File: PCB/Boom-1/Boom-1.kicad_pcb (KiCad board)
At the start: 2 copper layers, 698 parts, among them J1 NoiseIOConn, J10 Osc1HFTrackConn, J11 Osc1FiltCVConn, J12 OscFiltEnv1Conn, J13 OscFiltEnv2Conn, J14 SubFiltEnv1Conn, J15 SubFiltEnv2Conn, J16 Osc1FXConn, J17 SubFXConn, J18 Osc1FiltCVConn, J19 Osc1FiltCVConn, J2 Osc2CVConn, J20 Osc2FXConn, J21 OscAmpEnvConn, J22 SubAmpEnvConn, J23 OscAmpEnvBypass, J24 SubAmpAudioBypass, J25 SubAmpEnvBypass, J26 PreFV1FXConn, J27 PowerConn, J28 FV1Conn, J29 IOConn, J3 Osc1CVConn, J4 Osc2SyncConn, J5 Osc1SyncConn, J6 Osc2ScaleConn, J7 Osc2HFTrackConn, J8 SubIOConn, J9 Osc1ScaleConn, Q1 2N3904, SW1 SW_DIP_x04, U1 CEM3340, U10 AS3320, U11 AS3310, U12 AS3310, U13 AS3310, U14 AS3310, U15 V2164D, U16 AS3310, U17 AS3310, U18 V2164D, U19 TL074, U2 CEM3340, U20 TL074, U21 TL074, U22 TL074, U23 TL074, U24 TL074, U25 TL074, U26 TL074, U27 TL072, U28 TL074, U29 TL072, U3 4013, U30 TL074, U31 TL072, U32 TL074, U33 TL074, U34 TL074, U35 TL072, U36 TL074, U37 TL074, U38 TL072, U39 TL074, U4 NOISE, U40 TL072, U41 TL074, U42 TL074, U43 TL074, U44 TL074, U45 L7905, U46 L7805, U5 V2164D, U6 V2164D, U7 V2164D, U8 AS3320, U9 AS3320

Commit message: gathered up some stray parts
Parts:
- moved TP4 1583.4 mm to (-734.3, 189.5)
- moved R79 1444.9 mm to (-708.9, 138.4)
- moved R80 1426.5 mm to (-724.4, 378.7)
- moved R57 1421.4 mm to (-736.3, 372.4)
- moved R56 1403.7 mm to (-729.2, 369.1)
- moved R58 1394.2 mm to (-736.6, 378.7)
- moved R370 1292.9 mm to (-721.6, 403.1), turned to 180 degrees
- moved R292 813.4 mm to (2.29, 146.6)
- moved C106 42.6 mm to (751.1, 644.7)
- moved C138 42.6 mm to (754.9, 661.1)
- moved C148 42.6 mm to (769.2, 635.3)
- moved C149 42.6 mm to (767.9, 644.5)
- moved C163 42.6 mm to (735.1, 647.7)
- moved C171 42.6 mm to (736.0, 643.5)
- moved C40 42.6 mm to (764.0, 640.0)
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
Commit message: gathered up some rogue parts, started on the FX section components - pausing to update from schema
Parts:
- moved C41 1813.5 mm to (-730.5, -367.8)
- moved C40 1804.8 mm to (-721.1, -385.6)
- moved R100 1751.0 mm to (-739.1, -370.8)
- moved R131 1737.4 mm to (-691.9, -406.0)
- moved R99 1726.2 mm to (-728.5, -379.7)
- moved R186 1515.2 mm to (-483.9, -302.3)
- moved C54 1412.1 mm to (-400.6, -123.4)
- moved R142 1341.1 mm to (-403.6, -117.6)
- moved C111 1317.7 mm to (-503.2, 255.5), turned to 180 degrees
- moved R181 1309.8 mm to (-366.8, -99.8), turned to 180 degrees
- moved C112 1264.4 mm to (-483.6, 345.9), turned to 270 degrees
- moved C106 1243.8 mm to (-457.5, 350.8)
- moved C107 1240.9 mm to (-440.2, 350.8)
- moved C110 1233.3 mm to (-473.5, 249.4), turned to 270 degrees
- moved C101 1230.8 mm to (-439.9, 296.4)
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
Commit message: all parts are gathered from the swamp
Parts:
- moved C18 1357.0 mm to (-716.5, -341.5)
- moved C19 1289.3 mm to (-696.5, -345.1)
- moved C12 1270.9 mm to (-715.6, -132.0)
- moved C24 1248.0 mm to (-698.1, -102.5)
- moved C23 1225.3 mm to (-716.0, -100.7)
- moved C13 1217.0 mm to (-698.5, -132.1)
- moved C147 315.7 mm to (278.5, 27.9), turned to 90 degrees
- moved C149 311.5 mm to (295.0, 9.02), turned to 270 degrees
- moved R338 275.9 mm to (408.9, 18.3)
- moved R340 269.2 mm to (386.5, 1.40)
- moved R327 267.8 mm to (323.5, 0.00), turned to 180 degrees
- moved R365 263.7 mm to (511.2, 11.6)
- moved R337 259.9 mm to (410.7, 23.5)
- moved C172 258.9 mm to (496.1, 3.17), turned to 180 degrees
- moved R342 254.7 mm to (395.4, 6.99)
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
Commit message: osc1 layout
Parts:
- moved R109 79.6 mm to (-741.3, -358.9)
- moved D10 77.5 mm to (334.3, -67.9), turned to 90 degrees
- moved TP20 74.1 mm to (-750.1, -329.2)
- moved TP21 66.6 mm to (-746.0, -329.2)
- moved R371 61.1 mm to (-733.7, -347.6), turned to 180 degrees
- moved R114 59.7 mm to (-754.5, -343.0), turned to 180 degrees
- moved C43 51.4 mm to (-738.1, -369.2), turned to 270 degrees
- moved R85 51.3 mm to (-772.9, -404.4)
- moved R108 51.3 mm to (-741.3, -334.8)
- moved TP18 48.7 mm to (-746.4, -365.8)
- moved R132 48.5 mm to (-742.2, -409.4)
- moved R130 48.3 mm to (-744.5, -390.9)
- moved C51 48.2 mm to (-739.6, -406.1)
- moved U5 47.8 mm to (-751.7, -355.7)
- moved C41 47.7 mm to (-758.1, -328.8), turned to 90 degrees
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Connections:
- C51 pad 2: Net-(C51-Pad1) -> Net-(C51-Pad2)
- R108 pad 2: Net-(C51-Pad1) -> Net-(C51-Pad2)
- R109 pad 2: Net-(C51-Pad1) -> Net-(C51-Pad2)
- R132 pad 1: Net-(C51-Pad1) -> Net-(C51-Pad2)
- TP26 pad 1: Net-(C51-Pad1) -> Net-(C51-Pad2)
- U19 pad 14: Net-(C51-Pad1) -> Net-(C51-Pad2)

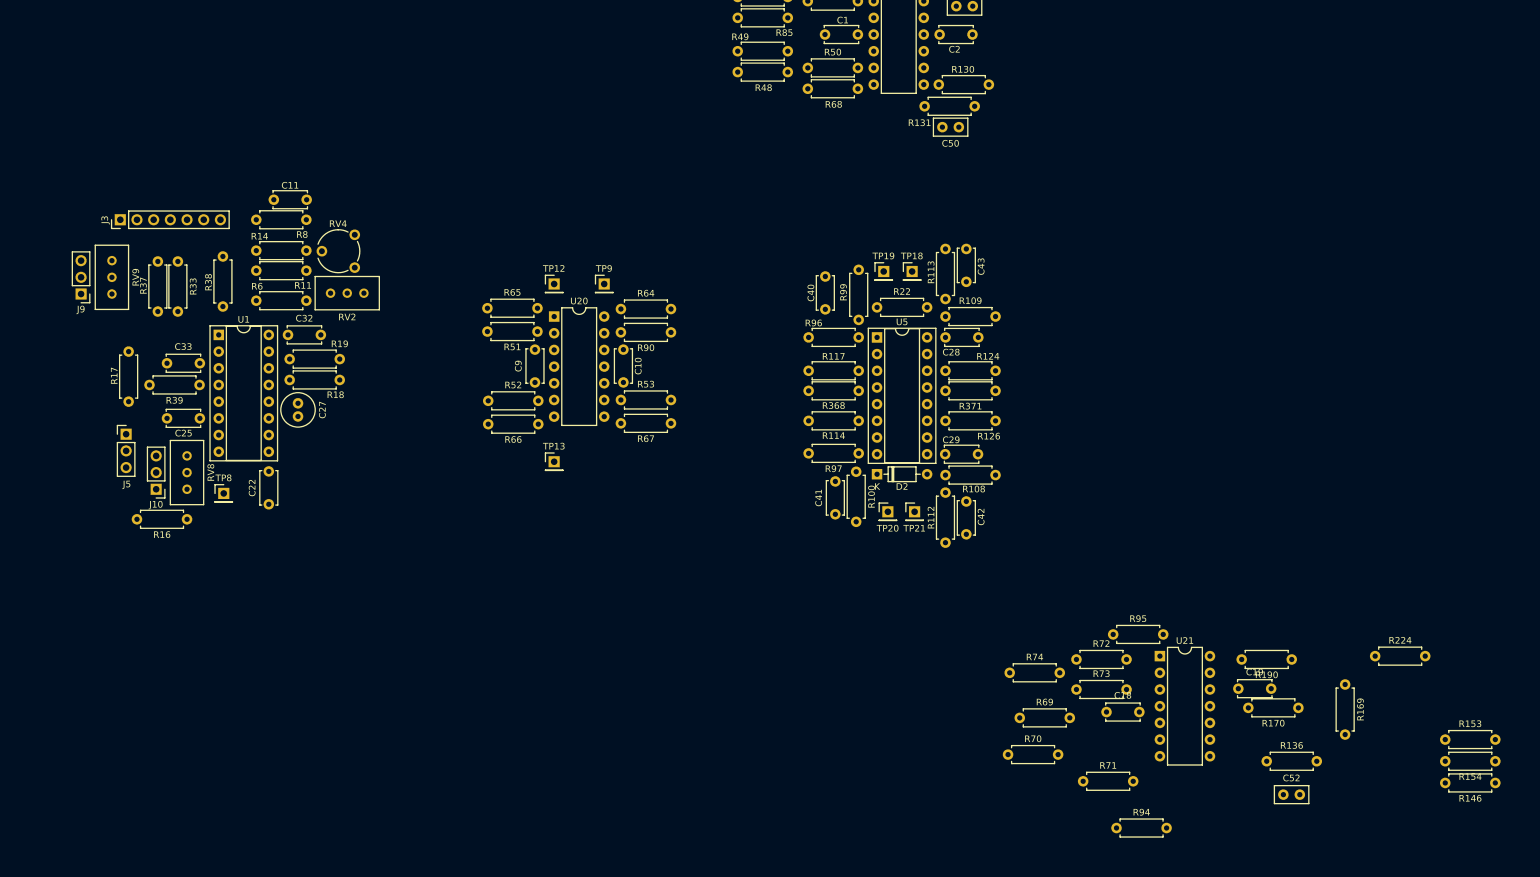
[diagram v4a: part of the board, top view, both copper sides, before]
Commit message: started adding traces to osc1
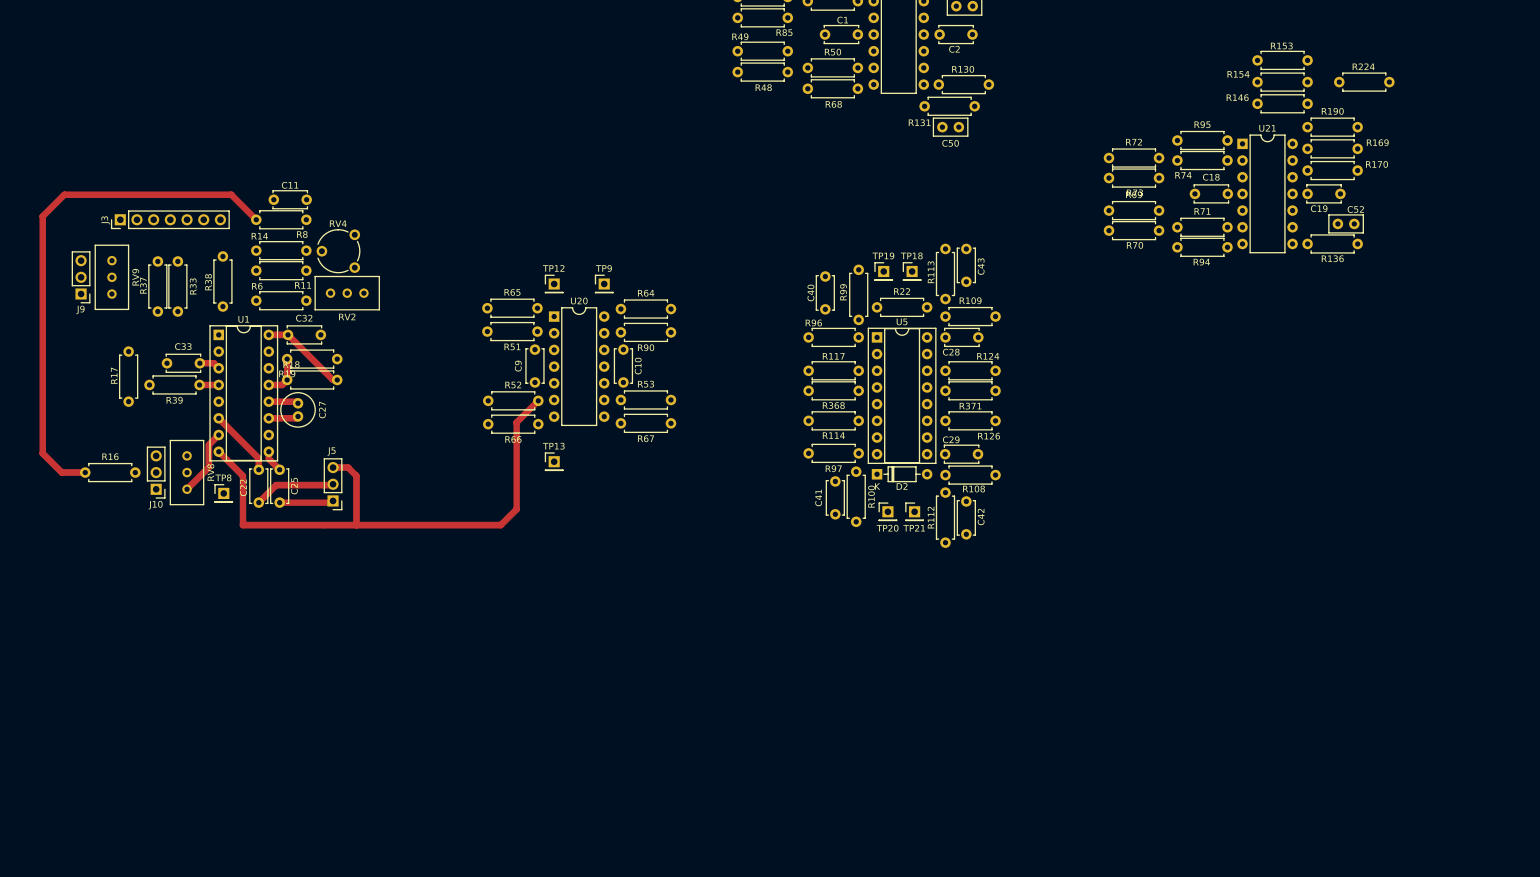
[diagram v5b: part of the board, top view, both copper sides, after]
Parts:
- moved R153 107.3 mm to (-693.8, -397.9)
- moved R146 107.3 mm to (-686.2, -391.3)
- moved R154 107.3 mm to (-686.2, -394.6)
- moved R94 88.9 mm to (-706.0, -369.4)
- moved C52 87.5 mm to (-679.1, -373.0), turned to 180 degrees
- moved R224 87.4 mm to (-673.7, -394.6), turned to 180 degrees
- moved R71 85.5 mm to (-706.0, -372.5)
- moved R74 82.0 mm to (-706.0, -382.7)
- moved R170 81.8 mm to (-686.2, -381.1), turned to 0 degrees
- moved R169 81.7 mm to (-686.2, -384.4), turned to 0 degrees
- moved R70 81.2 mm to (-716.4, -372.0)
- moved R190 81.1 mm to (-686.2, -387.7), turned to 0 degrees
- moved C18 80.0 mm to (-703.3, -377.6)
- moved R136 79.0 mm to (-686.2, -370.0)
- moved U21 79.0 mm to (-696.1, -385.2)
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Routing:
- net Net-(J5-Pad3): track 0.00 -> 84.8 mm
- net Net-(R11-Pad1): track 0.00 -> 79.2 mm
- net +12V: track 0.00 -> 13.3 mm
- net Net-(C25-Pad1): track 0.00 -> 12.5 mm
- net Net-(C25-Pad2): track 0.00 -> 10.4 mm
- net Net-(J10-Pad1): track 0.00 -> 10.3 mm
- net Net-(C22-Pad1): track 0.00 -> 8.23 mm
- net Net-(R18-Pad1): track 0.00 -> 6.28 mm
- net Net-(C27-Pad2): track 0.00 -> 4.56 mm
- net GND: track 0.00 -> 4.55 mm
- net Net-(C22-Pad2): track 0.00 -> 3.43 mm
- net -5V: track 0.00 -> 3.19 mm
- net Net-(R39-Pad1): track 0.00 -> 2.92 mm

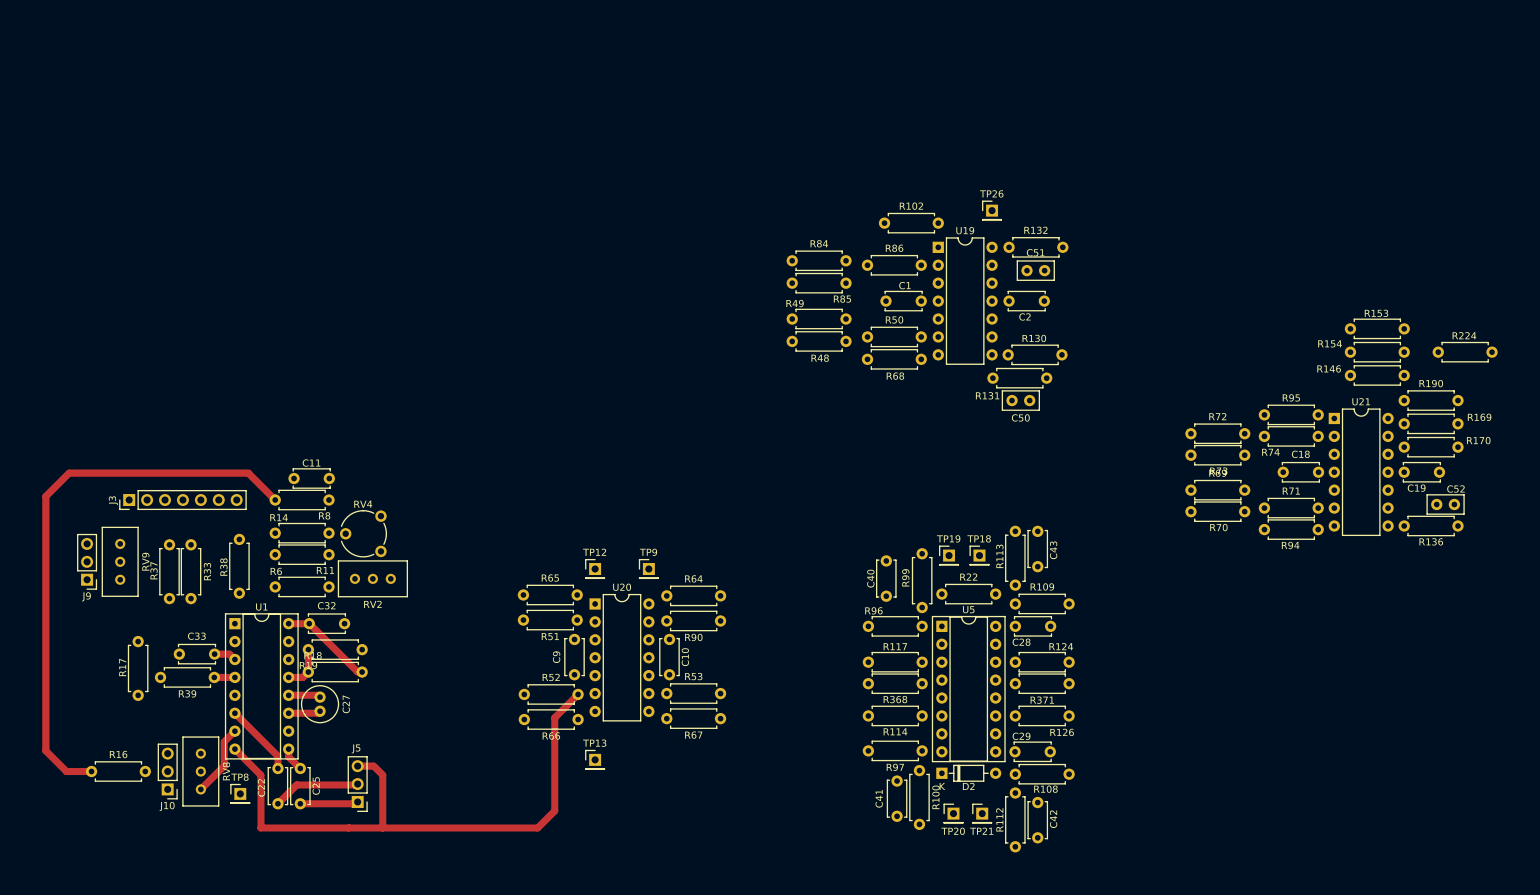
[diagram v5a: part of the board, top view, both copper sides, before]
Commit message: wiring up op amps in osc1
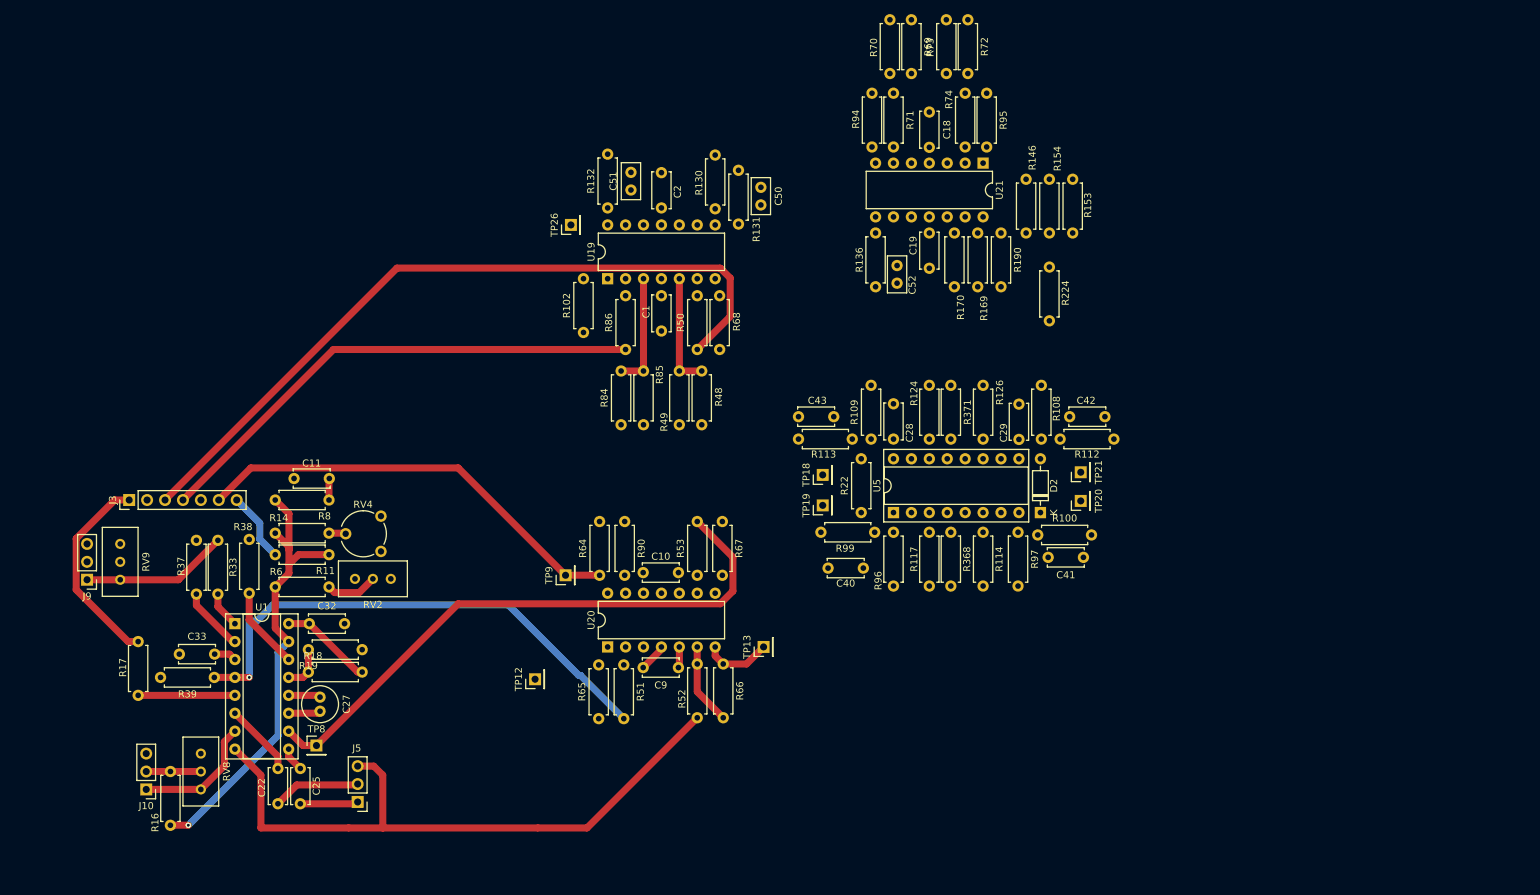
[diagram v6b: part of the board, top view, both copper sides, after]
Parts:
- moved R136 85.7 mm to (-761.1, -411.5), turned to 270 degrees
- moved C52 85.0 mm to (-758.1, -404.4), turned to 90 degrees
- moved R94 83.2 mm to (-761.6, -431.3), turned to 270 degrees
- moved R70 81.7 mm to (-759.1, -441.7), turned to 270 degrees
- moved R71 78.9 mm to (-758.6, -431.3), turned to 270 degrees
- moved R69 77.6 mm to (-756.0, -441.7), turned to 270 degrees
- moved C19 75.4 mm to (-753.5, -411.5), turned to 270 degrees
- moved C18 71.6 mm to (-753.5, -428.6), turned to 270 degrees
- moved R73 70.8 mm to (-751.1, -441.7), turned to 270 degrees
- moved R170 70.6 mm to (-749.9, -411.5), turned to 270 degrees
- moved R72 66.7 mm to (-748.0, -441.7), turned to 270 degrees
- moved R169 66.2 mm to (-746.6, -411.5), turned to 270 degrees
- moved R74 64.5 mm to (-748.4, -431.3), turned to 270 degrees
- moved R224 62.9 mm to (-736.5, -399.0), turned to 90 degrees
- moved R190 61.9 mm to (-743.3, -411.5), turned to 270 degrees
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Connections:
- R11 pad 2: Net-(J3-Pad4) -> Net-(J3-Pad7)
- R17 pad 1: Net-(J3-Pad5) -> Net-(J3-Pad1)
- R50 pad 1: Net-(J3-Pad6) -> Net-(J3-Pad3)
- R64 pad 1: Net-(J3-Pad3) -> Net-(J3-Pad6)
- R71 pad 1: Net-(J3-Pad1) -> Net-(J3-Pad5)
- R86 pad 1: Net-(J3-Pad7) -> Net-(J3-Pad4)
- TP9 pad 1: Net-(J3-Pad3) -> Net-(J3-Pad6)
- U20 pad 14: Net-(J3-Pad3) -> Net-(J3-Pad6)
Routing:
- net Net-(J3-Pad3): track 0.00 -> 106.4 mm
- net Net-(R53-Pad2): track 0.00 -> 84.8 mm
- net Net-(J3-Pad4): track 0.00 -> 71.6 mm
- net Net-(R39-Pad1): track 2.92 -> 73.7 mm, vias 0 -> 1
- net Net-(J3-Pad6): track 0.00 -> 62.2 mm
- net Net-(J3-Pad1): track 0.00 -> 28.9 mm
- net Net-(J9-Pad1): track 0.00 -> 20.9 mm
- net Net-(R84-Pad2): track 0.00 -> 16.3 mm
- net Net-(R48-Pad2): track 0.00 -> 16.3 mm
- net Net-(R17-Pad2): track 0.00 -> 13.7 mm
- net Net-(R11-Pad1): track 79.2 -> 66.3 mm, vias 0 -> 1
- net Net-(R38-Pad2): track 0.00 -> 11.7 mm
- net Net-(R52-Pad1): track 0.00 -> 11.6 mm
- net Net-(J3-Pad7): track 0.00 -> 10.0 mm
- net Net-(R66-Pad1): track 0.00 -> 9.60 mm
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
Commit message: trying more layouts
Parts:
- moved R190 10.9 mm to (-732.9, -408.4), turned to 180 degrees
- moved C1 4.95 mm to (-791.5, -397.6), turned to 90 degrees
- moved R153 4.06 mm to (-729.1, -419.1)
- moved R146 4.06 mm to (-735.7, -411.5)
- moved R154 4.06 mm to (-732.4, -411.5)
- moved R224 2.67 mm to (-736.5, -396.4)
- moved C51 2.55 mm to (-796.0, -420.1), turned to 270 degrees
- moved R169 2.42 mm to (-746.8, -409.1)
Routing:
- net Net-(R146-Pad2): track 0.00 -> 31.6 mm
- net Net-(C51-Pad1): track 0.00 -> 26.2 mm
- net Net-(R190-Pad1): track 0.00 -> 19.3 mm
- net Net-(R72-Pad2): track 0.00 -> 15.8 mm
- net Net-(R69-Pad2): track 0.00 -> 15.7 mm
- net Net-(C50-Pad1): track 0.00 -> 14.3 mm
- net Net-(C52-Pad1): track 0.00 -> 14.1 mm
- net Net-(C51-Pad2): track 0.00 -> 11.7 mm
- net Net-(R71-Pad2): track 0.00 -> 11.2 mm
- net Net-(R74-Pad2): track 0.00 -> 11.2 mm
- net Net-(C50-Pad2): track 0.00 -> 9.94 mm
- net Net-(C52-Pad2): track 0.00 -> 8.16 mm
- net Net-(R102-Pad1): track 0.00 -> 8.13 mm
- net Net-(R169-Pad1): track 0.00 -> 6.88 mm
- net Net-(R102-Pad2): track 0.00 -> 3.43 mm
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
